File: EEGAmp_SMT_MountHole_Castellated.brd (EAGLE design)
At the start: 25.5 x 11.2 mm, 15 parts, among them U1 TL084QD

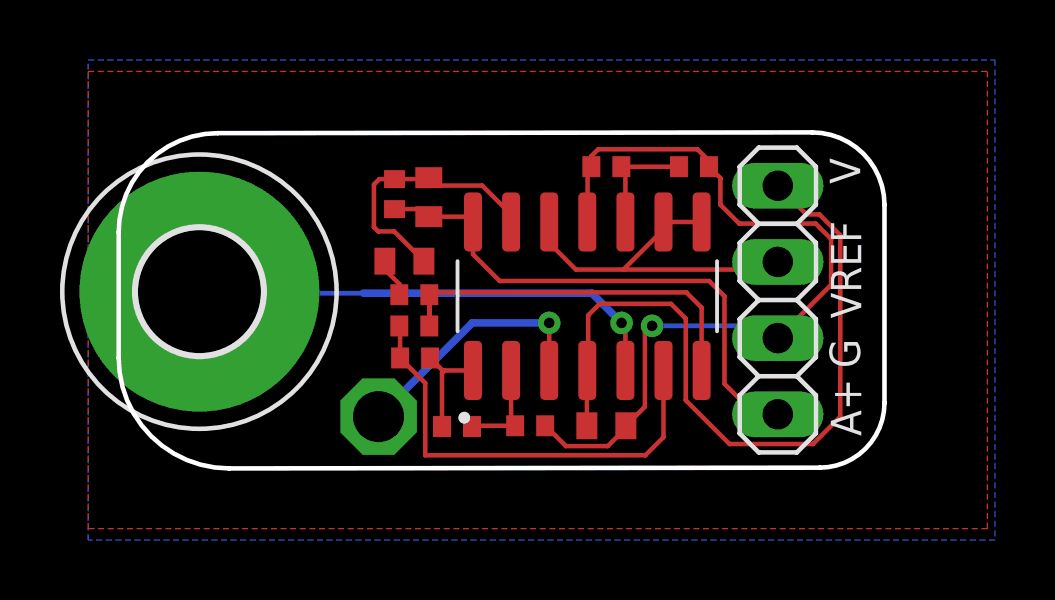
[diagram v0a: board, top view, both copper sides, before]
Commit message: separate castellated mounthole and non castellated, more screenshots/links.
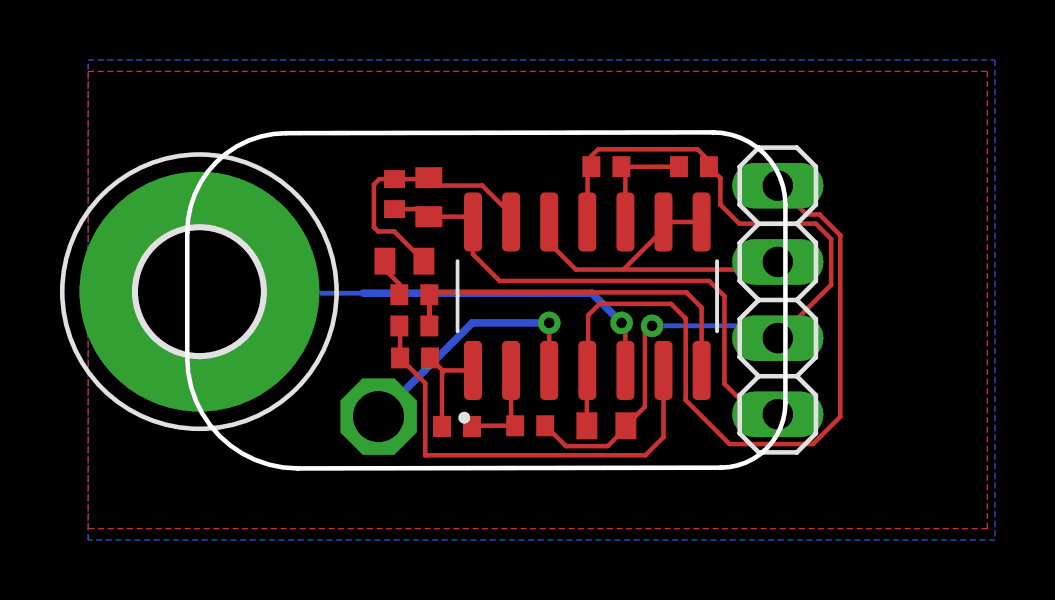
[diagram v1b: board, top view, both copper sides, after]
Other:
- board size 25.5 x 11.2 mm -> 19.9 x 11.2 mm
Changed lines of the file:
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@@
 <text x="18.542" y="28.956" size="1.778" layer="26" rot="MR0">+</text>
 <text x="18.360284375" y="20.109" size="1.778" layer="26" rot="MR0">--</text>
-<text x="35.767296875" y="29.145721875" size="1.016" layer="25" rot="R90">V</text>
-<text x="35.802071875" y="24.661759375" size="1.016" layer="25" rot="R90">VREF</text>
-<text x="35.76176875" y="23.005471875" size="1.016" layer="25" rot="R90">G</text>
-<text x="35.802465625" y="20.74333125" size="1.016" layer="25" rot="R90">A+</text>
-<wire x1="11.049" y1="27.5336" x2="14.351" y2="30.8356" width="0.1524" layer="20" curve="-90"/>
-<wire x1="14.351" y1="30.8356" x2="34.163" y2="30.861" width="0.1524" layer="20"/>
-<wire x1="34.163" y1="30.861" x2="36.576" y2="28.448" width="0.1524" layer="20" curve="-90"/>
-<wire x1="36.576" y1="28.448" x2="36.576" y2="21.844" width="0.1524" layer="20"/>
-<wire x1="36.576" y1="21.844" x2="34.417" y2="19.685" width="0.1524" layer="20" curve="-90"/>
-<wire x1="34.417" y1="19.685" x2="14.732" y2="19.6596" width="0.1524" layer="20"/>
-<wire x1="14.732" y1="19.6596" x2="11.049" y2="23.3426" width="0.1524" layer="20" curve="-90"/>
-<wire x1="11.049" y1="23.3426" x2="11.049" y2="27.5336" width="0.1524" layer="20"/>
+<text x="29.764703125" y="29.145721875" size="1.016" layer="26" rot="MR90">V</text>
+<text x="29.729928125" y="24.661759375" size="1.016" layer="26" rot="MR90">VREF</text>
+<text x="29.77023125" y="23.005471875" size="1.016" layer="26" rot="MR90">G</text>
+<text x="29.729534375" y="20.74333125" size="1.016" layer="26" rot="MR90">A+</text>
+<wire x1="13.335" y1="27.5336" x2="16.637" y2="30.8356" width="0.1524" layer="20" curve="-90"/>
+<wire x1="16.637" y1="30.8356" x2="30.861" y2="30.861" width="0.1524" layer="20"/>
+<wire x1="30.861" y1="30.861" x2="33.274" y2="28.448" width="0.1524" layer="20" curve="-90"/>
+<wire x1="33.274" y1="28.448" x2="33.274" y2="21.844" width="0.1524" layer="20"/>
+<wire x1="33.274" y1="21.844" x2="31.115" y2="19.685" width="0.1524" layer="20" curve="-90"/>
+<wire x1="31.115" y1="19.685" x2="17.018" y2="19.6596" width="0.1524" layer="20"/>
+<wire x1="17.018" y1="19.6596" x2="13.335" y2="23.3426" width="0.1524" layer="20" curve="-90"/>
+<wire x1="13.335" y1="23.3426" x2="13.335" y2="27.5336" width="0.1524" layer="20"/>
 <dimension x1="34.163" y1="30.861" x2="34.417" y2="19.685" x3="39.37" y3="25.273" textsize="1.778" layer="47" dtype="vertical"/>
 <circle x="13.7693375" y="25.6057375" radius="4.999521875" width="0.1524" layer="51"/>
 <circle x="13.756640625" y="25.5651" radius="1.955146875" width="0.1524" layer="51"/>
-<dimension x1="11.049" y1="27.5336" x2="36.576" y2="28.448" x3="23.8125" y3="35.56" textsize="1.778" layer="47" dtype="horizontal"/>
+<dimension x1="13.335" y1="27.5336" x2="33.274" y2="28.448" x3="23.3045" y3="35.052" textsize="1.778" layer="47" dtype="horizontal"/>
 </plain>
 <attributes>

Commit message: add centroids
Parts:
- moved AIN- 1.70 mm to (19.7, 19.7)
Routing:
- net AIN-: track 8.57 -> 10.1 mm
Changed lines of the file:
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@@
 <setting verticaltext="up"/>
 </settings>
-<grid distance="10" unitdist="mil" unit="mil" style="lines" multiple="1" display="no" altdistance="5" altunitdist="mil" altunit="mil"/>
+<grid distance="1" unitdist="mil" unit="mil" style="lines" multiple="1" display="no" altdistance="5" altunitdist="mil" altunit="mil"/>
 <layers>
 <layer number="1" name="Top" color="4" fill="1" visible="yes" active="yes"/>
@@
 <attribute name="VALUE" x="29.845" y="30.353" size="1.27" layer="27" rot="R270"/>
 </element>
-<element name="AIN-" library="testpad" library_urn="urn:adsk.eagle:library:385" package="P1-17" package3d_urn="urn:adsk.eagle:package:27949/1" value="PTR1PAD1-17" x="19.7104" y="21.3868" smashed="yes" rot="R90">
-<attribute name="POPULARITY" value="0" x="19.7104" y="21.3868" size="1.778" layer="27" rot="R90" display="off"/>
-<attribute name="TP_SIGNAL_NAME" value="" x="19.7104" y="21.3868" size="1.778" layer="27" rot="R90" display="off"/>
+<element name="AIN-" library="testpad" library_urn="urn:adsk.eagle:library:385" package="P1-17" package3d_urn="urn:adsk.eagle:package:27949/1" value="PTR1PAD1-17" x="19.7104" y="19.685" smashed="yes" rot="R90">
+<attribute name="POPULARITY" value="0" x="19.7104" y="19.685" size="1.778" layer="27" rot="R90" display="off"/>
+<attribute name="TP_SIGNAL_NAME" value="" x="19.7104" y="19.685" size="1.778" layer="27" rot="R90" display="off"/>
 </element>
 <element name="H1" library="holes" package="4,1-PAD" value="MOUNT-PAD-ROUND4.1" x="13.7414" y="25.5524" smashed="yes"/>
@@
 <wire x1="25.4" y1="24.511" x2="25.4" y2="22.925" width="0.1524" layer="1"/>
 <contactref element="AIN-" pad="TP"/>
-<wire x1="19.7104" y1="21.3868" x2="22.8346" y2="24.511" width="0.254" layer="16"/>
-<wire x1="22.8346" y1="24.511" x2="25.4" y2="24.511" width="0.254" layer="16"/>
+<wire x1="23.0886" y1="24.511" x2="19.7104" y2="21.1328" width="0.254" layer="16"/>
+<wire x1="19.7104" y1="19.685" x2="19.7104" y2="21.1328" width="0.254" layer="16"/>
+<wire x1="23.0886" y1="24.511" x2="25.4" y2="24.511" width="0.254" layer="16"/>
 </signal>
 <signal name="VREF">
@@
 <wire x1="27.94" y1="24.384" x2="27.94" y2="22.925" width="0.1524" layer="1"/>
 <wire x1="27.813" y1="24.511" x2="26.8224" y2="25.5016" width="0.254" layer="16"/>
-<wire x1="26.8224" y1="25.5016" x2="19.2024" y2="25.5016" width="0.254" layer="16"/>
 <contactref element="H1" pad="B4,1"/>
-<wire x1="19.2024" y1="25.5016" x2="13.7922" y2="25.5016" width="0.1524" layer="16"/>
 <wire x1="13.7922" y1="25.5016" x2="13.7414" y2="25.5524" width="0.1524" layer="16"/>
+<wire x1="26.8224" y1="25.5016" x2="13.7922" y2="25.5016" width="0.254" layer="16"/>
 </signal>
 <signal name="2IN-">

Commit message: fixed, smaller
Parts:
- moved R5 1.45 mm to (28.8, 29.7)
- moved R6 0.76 mm to (26.5, 29.7)
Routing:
- net VDD: track 25.0 -> 12.2 mm, vias 0 -> 1
- net GND: track 27.6 -> 24.7 mm, vias 1 -> 2
- net VREF: track 12.2 -> 11.3 mm

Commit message: fixed reference circuit (oops)
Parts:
- added REFOUT: PTR1PAD1-17, testpad:P1-17
- moved C2 2.45 mm to (23.6, 29.6), turned to 180 degrees
- moved R8 1.25 mm to (21.4, 29.2)
- moved AIN- 0.64 mm to (19.1, 19.7)
- moved C1 0.34 mm to (20.9, 26.5)
- moved JP2 0.10 mm to (33.1, 25.3)
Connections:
- new net REFOUT: REFOUT.TP, U1.12, U1.8, U1.9
- net GND: no longer R5.2
- net VREF: now also R5.2; no longer U1.12, U1.8, U1.9
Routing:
- net REFOUT: track 0.00 -> 19.1 mm, vias 0 -> 1
- net VREF: track 11.3 -> 6.49 mm
- net GND: track 24.7 -> 27.2 mm, vias 2 -> 1
- net VDD: track 12.2 -> 13.1 mm
- net AOUT: track 18.2 -> 18.8 mm
- net VOD: track 13.3 -> 12.7 mm
